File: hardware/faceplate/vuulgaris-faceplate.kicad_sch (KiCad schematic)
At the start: 7 parts, among them J1 HX JN2.54-2x5P TP H8.9, U1 MSP430FR2675TPT

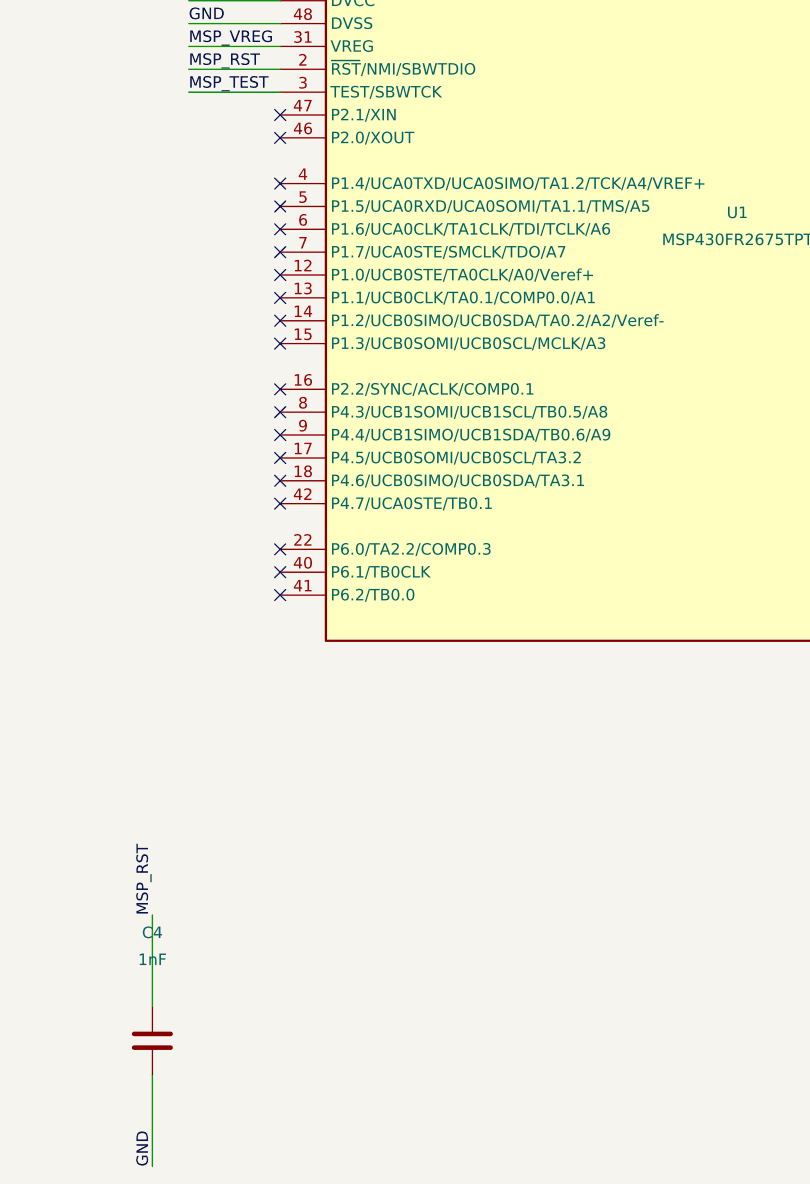
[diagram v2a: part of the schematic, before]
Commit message: faceplate: UART on P1.4/P1.5 with 47k pull-ups
U1 pin 4 (P1.4/UCA0TXD) on MSP430_TXD and pin 5 (P1.5/UCA0RXD) on
MSP430_RXD, the cable's J1.7 and J1.5 -- the default UCA0 pins, which are
also the UART BSL's (SLASEO5D Table 9-4, pin-allocation.md).

From TI: R2/R3 47k pull-ups, SLAU550 section 3.3.2.1, "Add a 47-kohm pullup
resistor and a 1-nF pulldown capacitor on TCK and TMS" (P1.4 is TCK, P1.5
TMS). Not fitted, by the decision in README section 6: the 1nF pulldowns,
which serve the hardware BSL entry sequence that production never uses.

Checked: mksch -> netcheck 31/31, 0 unintended, 7 nets; panelcheck 6 OK;
board untouched.
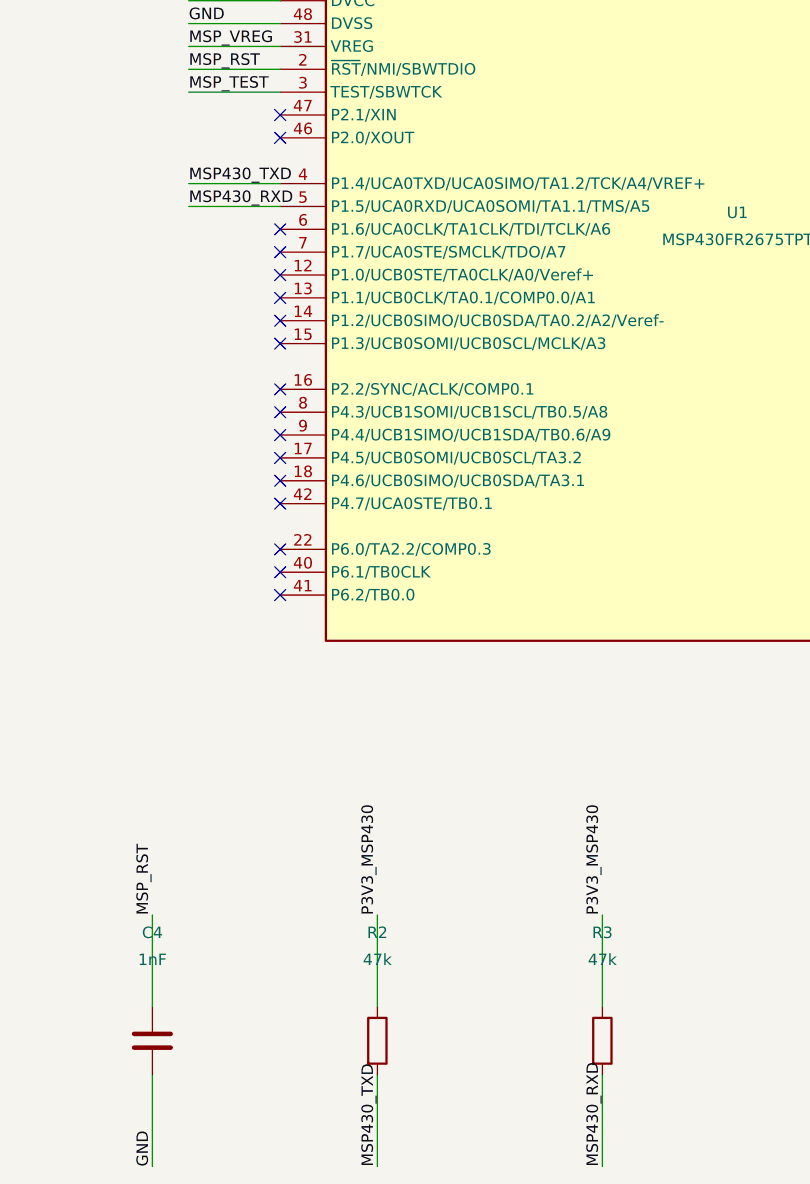
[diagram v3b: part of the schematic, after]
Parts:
- added R2, R3: 47k, vuulgaris:R0603, symbol vuulgaris:R
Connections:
- net MSP430_RXD: now also U1.5 (P1.5/UCA0RXD/UCA0SOMI/TA1.1/TMS/A5), R3.2
- net MSP430_TXD: now also U1.4 (P1.4/UCA0TXD/UCA0SIMO/TA1.2/TCK/A4/VREF+), R2.2
- net P3V3_MSP430: now also R2.1, R3.1
- no-connect marks 43 -> 41
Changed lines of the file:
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@@
+    (pin "2")
+  )
+  (symbol (lib_id "vuulgaris:R") (at 290 300 0) (unit 1)
+    (in_bom yes) (on_board yes) (dnp no)
+    (property "Reference" "R2" (at 290 288 0) (effects (font (size 1.27 1.27))))
+    (property "Value" "47k" (at 290 291 0) (effects (font (size 1.27 1.27))))
+    (property "Footprint" "vuulgaris:R0603" (at 290 300 0) (effects (font (size 1.27 1.27)) hide))
+    (property "Datasheet" "" (at 290 300 0) (effects (font (size 1.27 1.27)) hide))
+    (pin "1")
+    (pin "2")
+  )
+  (symbol (lib_id "vuulgaris:R") (at 315 300 0) (unit 1)
+    (in_bom yes) (on_board yes) (dnp no)
+    (property "Reference" "R3" (at 315 288 0) (effects (font (size 1.27 1.27))))
+    (property "Value" "47k" (at 315 291 0) (effects (font (size 1.27 1.27))))
+    (property "Footprint" "vuulgaris:R0603" (at 315 300 0) (effects (font (size 1.27 1.27)) hide))
+    (property "Datasheet" "" (at 315 300 0) (effects (font (size 1.27 1.27)) hide))
+    (pin "1")
     (pin "2")
   )
@@
   (wire (pts (xy 240.0 296.19) (xy 240.0 286.03)) (stroke (width 0) (type solid)))
   (wire (pts (xy 240.0 303.81) (xy 240.0 313.97)) (stroke (width 0) (type solid)))
+  (wire (pts (xy 290.0 296.19) (xy 290.0 286.03)) (stroke (width 0) (type solid)))
+  (wire (pts (xy 290.0 303.81) (xy 290.0 313.97)) (stroke (width 0) (type solid)))
+  (wire (pts (xy 315.0 296.19) (xy 315.0 286.03)) (stroke (width 0) (type solid)))
+  (wire (pts (xy 315.0 303.81) (xy 315.0 313.97)) (stroke (width 0) (type solid)))
   (wire (pts (xy 279.2 184.44) (xy 269.04 184.44)) (stroke (width 0) (type solid)))
   (wire (pts (xy 279.2 186.98) (xy 269.04 186.98)) (stroke (width 0) (type solid)))
@@
   (wire (pts (xy 279.2 192.06) (xy 269.04 192.06)) (stroke (width 0) (type solid)))
   (wire (pts (xy 279.2 194.6) (xy 269.04 194.6)) (stroke (width 0) (type solid)))
+  (wire (pts (xy 279.2 204.76) (xy 269.04 204.76)) (stroke (width 0) (type solid)))
+  (wire (pts (xy 279.2 207.3) (xy 269.04 207.3)) (stroke (width 0) (type solid)))
   (label "P3V3_MSP430" (at 160.0 286.03 90) (fields_autoplaced)
     (effects (font (size 1.27 1.27)) (justify left bottom))
@@
     (effects (font (size 1.27 1.27)) (justify left bottom))
   )
+  (label "P3V3_MSP430" (at 290.0 286.03 90) (fields_autoplaced)
+    (effects (font (size 1.27 1.27)) (justify left bottom))
+  )
+  (label "MSP430_TXD" (at 290.0 313.97 270) (fields_autoplaced)
+    (effects (font (size 1.27 1.27)) (justify left bottom))
+  )
+  (label "P3V3_MSP430" (at 315.0 286.03 90) (fields_autoplaced)
+    (effects (font (size 1.27 1.27)) (justify left bottom))
+  )
+  (label "MSP430_RXD" (at 315.0 313.97 270) (fields_autoplaced)
+    (effects (font (size 1.27 1.27)) (justify left bottom))
+  )
   (label "P3V3_MSP430" (at 269.04 184.44 180) (fields_autoplaced)
     (effects (font (size 1.27 1.27)) (justify left bottom))
@@
   )
   (label "MSP_TEST" (at 269.04 194.6 180) (fields_autoplaced)
+    (effects (font (size 1.27 1.27)) (justify left bottom))
+  )
+  (label "MSP430_TXD" (at 269.04 204.76 180) (fields_autoplaced)
+    (effects (font (size 1.27 1.27)) (justify left bottom))
+  )
+  (label "MSP430_RXD" (at 269.04 207.3 180) (fields_autoplaced)
     (effects (font (size 1.27 1.27)) (justify left bottom))
   )
   (no_connect (at 279.2 197.14))
   (no_connect (at 279.2 199.68))
-  (no_connect (at 279.2 204.76))
-  (no_connect (at 279.2 207.3))
   (no_connect (at 279.2 209.84))
   (no_connect (at 279.2 212.38))

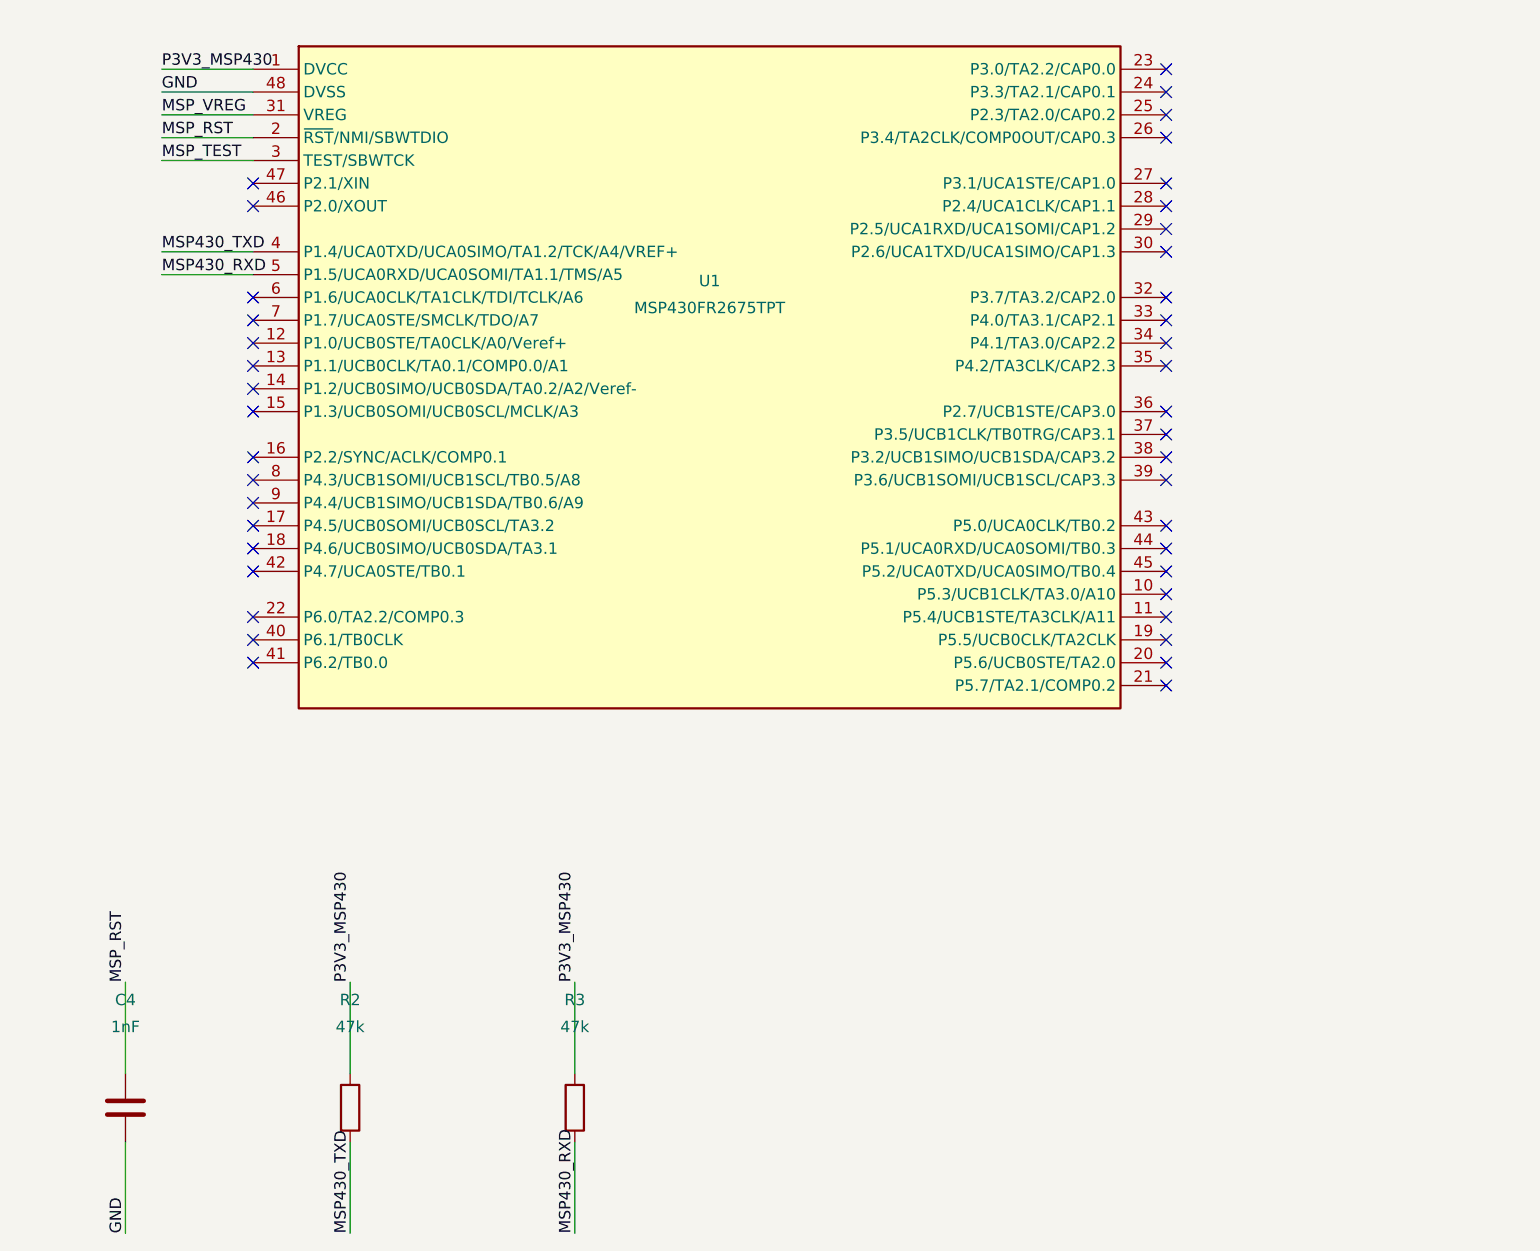
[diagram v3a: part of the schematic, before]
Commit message: faceplate: 32.768kHz crystal on XIN/XOUT (Q22)
Y1, Epson FC-135 32.768kHz 12.5pF (C32346, JLC Basic), on U1 pins 47
(P2.1/XIN) and 46 (P2.0/XOUT), C5/C6 22pF C0G from each pin to ground.

From a TI reference circuit: the topology, SLASEO5D section 10.1.2 /
Figure 10-2 -- crystal across XIN/XOUT, a capacitor from each to ground,
"External bypass capacitors for the crystal oscillator pins are required".
The crystal meets TI's limits in 8.12.3.1: a supported 12.5pF load, and C0
1pF against the 1.6pF maximum shunt capacitance.

NOT from a reference circuit: the capacitor value. TI gives none, only "meet
the effective load capacitance specified by crystal manufacturers", with
CL,eff 1pF integrated (8.12.3.1, read from the rendered table). 12.5pF less
1pF, doubled, less board stray is about 20pF; there is no Basic 20pF C0G 0603
at JLC (checked), so 22pF (C1653, already on the main board), a pF or so
high -- a few ppm of pull, irrelevant to a UART. Q22 updated; populating it
is still a later decision.

Checked: mksch -> netcheck 39/39, 0 unintended, 9 nets. Board untouched.
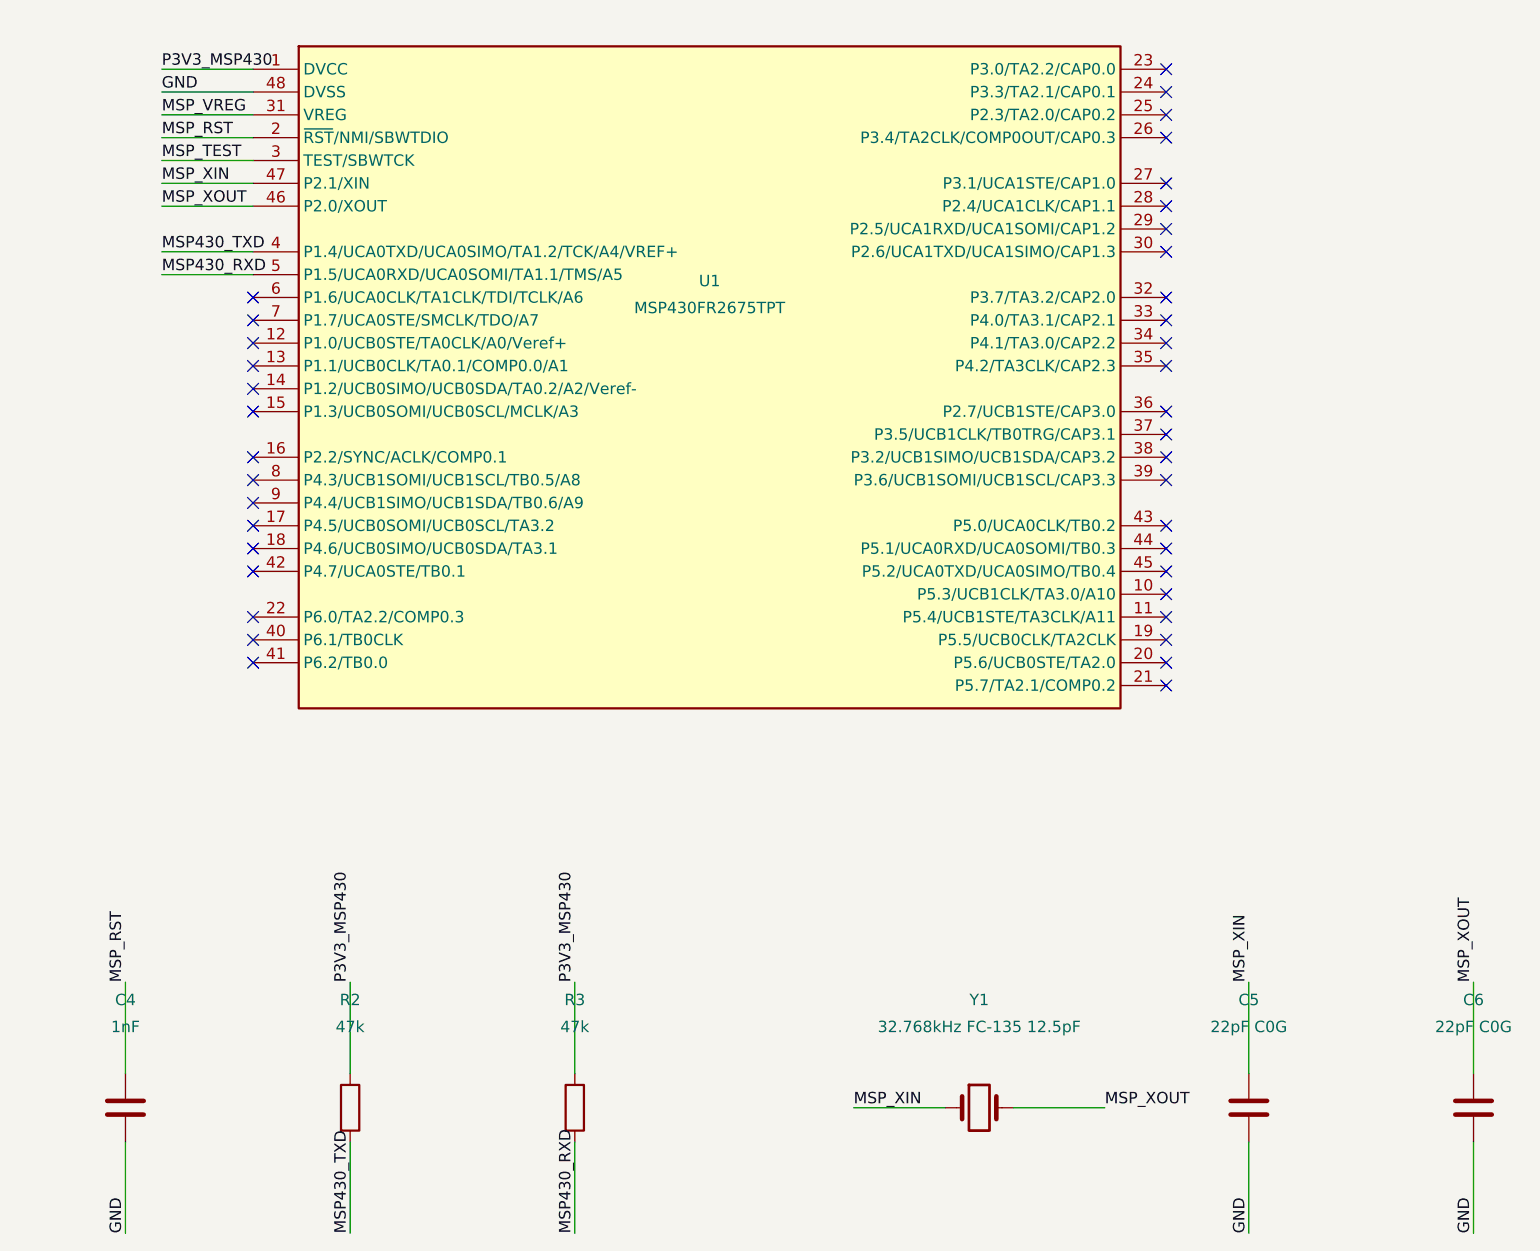
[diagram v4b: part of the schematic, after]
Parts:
- added C5, C6: 22pF C0G, vuulgaris:C0603, symbol vuulgaris:C
- added Y1: 32.768kHz FC-135 12.5pF, vuulgaris:XTAL-SMD_FC-135_3.2x1.5mm, symbol vuulgaris:Crystal
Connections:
- net GND: now also C5.2, C6.2
- net MSP_XOUT: now reaches U1.46 (P2.0/XOUT)
- net MSP_XOUT: now also C6.1, Y1.2
- net MSP_XIN: now reaches U1.47 (P2.1/XIN)
- net MSP_XIN: now also C5.1, Y1.1
- no-connect marks 41 -> 39
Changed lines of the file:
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@@
+    (pin "2")
+  )
+  (symbol (lib_id "vuulgaris:C") (at 390 300 0) (unit 1)
+    (in_bom yes) (on_board yes) (dnp no)
+    (property "Reference" "C5" (at 390 288 0) (effects (font (size 1.27 1.27))))
+    (property "Value" "22pF C0G" (at 390 291 0) (effects (font (size 1.27 1.27))))
+    (property "Footprint" "vuulgaris:C0603" (at 390 300 0) (effects (font (size 1.27 1.27)) hide))
+    (property "Datasheet" "" (at 390 300 0) (effects (font (size 1.27 1.27)) hide))
+    (pin "1")
+    (pin "2")
+  )
+  (symbol (lib_id "vuulgaris:C") (at 415 300 0) (unit 1)
+    (in_bom yes) (on_board yes) (dnp no)
+    (property "Reference" "C6" (at 415 288 0) (effects (font (size 1.27 1.27))))
+    (property "Value" "22pF C0G" (at 415 291 0) (effects (font (size 1.27 1.27))))
+    (property "Footprint" "vuulgaris:C0603" (at 415 300 0) (effects (font (size 1.27 1.27)) hide))
+    (property "Datasheet" "" (at 415 300 0) (effects (font (size 1.27 1.27)) hide))
+    (pin "1")
     (pin "2")
   )
@@
     (pin "21")
   )
+  (symbol (lib_id "vuulgaris:Crystal") (at 360 300 0) (unit 1)
+    (in_bom yes) (on_board yes) (dnp no)
+    (property "Reference" "Y1" (at 360 288 0) (effects (font (size 1.27 1.27))))
+    (property "Value" "32.768kHz FC-135 12.5pF" (at 360 291 0) (effects (font (size 1.27 1.27))))
+    (property "Footprint" "vuulgaris:XTAL-SMD_FC-135_3.2x1.5mm" (at 360 300 0) (effects (font (size 1.27 1.27)) hide))
+    (property "Datasheet" "" (at 360 300 0) (effects (font (size 1.27 1.27)) hide))
+    (pin "1")
+    (pin "2")
+  )
   (wire (pts (xy 160.0 296.19) (xy 160.0 286.03)) (stroke (width 0) (type solid)))
   (wire (pts (xy 160.0 303.81) (xy 160.0 313.97)) (stroke (width 0) (type solid)))
@@
   (wire (pts (xy 265.0 296.19) (xy 265.0 286.03)) (stroke (width 0) (type solid)))
   (wire (pts (xy 265.0 303.81) (xy 265.0 313.97)) (stroke (width 0) (type solid)))
+  (wire (pts (xy 390.0 296.19) (xy 390.0 286.03)) (stroke (width 0) (type solid)))
+  (wire (pts (xy 390.0 303.81) (xy 390.0 313.97)) (stroke (width 0) (type solid)))
+  (wire (pts (xy 415.0 296.19) (xy 415.0 286.03)) (stroke (width 0) (type solid)))
+  (wire (pts (xy 415.0 303.81) (xy 415.0 313.97)) (stroke (width 0) (type solid)))
   (wire (pts (xy 94.92 94.92) (xy 84.76 94.92)) (stroke (width 0) (type solid)))
   (wire (pts (xy 107.62 94.92) (xy 117.78 94.92)) (stroke (width 0) (type solid)))
@@
   (wire (pts (xy 279.2 204.76) (xy 269.04 204.76)) (stroke (width 0) (type solid)))
   (wire (pts (xy 279.2 207.3) (xy 269.04 207.3)) (stroke (width 0) (type solid)))
+  (wire (pts (xy 279.2 197.14) (xy 269.04 197.14)) (stroke (width 0) (type solid)))
+  (wire (pts (xy 279.2 199.68) (xy 269.04 199.68)) (stroke (width 0) (type solid)))
+  (wire (pts (xy 356.19 300.0) (xy 346.03 300.0)) (stroke (width 0) (type solid)))
+  (wire (pts (xy 363.81 300.0) (xy 373.97 300.0)) (stroke (width 0) (type solid)))
   (label "P3V3_MSP430" (at 160.0 286.03 90) (fields_autoplaced)
     (effects (font (size 1.27 1.27)) (justify left bottom))
@@
     (effects (font (size 1.27 1.27)) (justify left bottom))
   )
+  (label "MSP_XIN" (at 390.0 286.03 90) (fields_autoplaced)
+    (effects (font (size 1.27 1.27)) (justify left bottom))
+  )
+  (label "GND" (at 390.0 313.97 270) (fields_autoplaced)
+    (effects (font (size 1.27 1.27)) (justify left bottom))
+  )
+  (label "MSP_XOUT" (at 415.0 286.03 90) (fields_autoplaced)
+    (effects (font (size 1.27 1.27)) (justify left bottom))
+  )
+  (label "GND" (at 415.0 313.97 270) (fields_autoplaced)
+    (effects (font (size 1.27 1.27)) (justify left bottom))
+  )
   (label "MSP_TEST" (at 84.76 94.92 180) (fields_autoplaced)
     (effects (font (size 1.27 1.27)) (justify left bottom))
@@
     (effects (font (size 1.27 1.27)) (justify left bottom))
   )
-  (no_connect (at 279.2 197.14))
-  (no_connect (at 279.2 199.68))
+  (label "MSP_XIN" (at 269.04 197.14 180) (fields_autoplaced)
+    (effects (font (size 1.27 1.27)) (justify left bottom))
+  )
+  (label "MSP_XOUT" (at 269.04 199.68 180) (fields_autoplaced)
+    (effects (font (size 1.27 1.27)) (justify left bottom))
+  )
+  (label "MSP_XIN" (at 346.03 300.0 180) (fields_autoplaced)
+    (effects (font (size 1.27 1.27)) (justify left bottom))
+  )
+  (label "MSP_XOUT" (at 373.97 300.0 0) (fields_autoplaced)
+    (effects (font (size 1.27 1.27)) (justify left bottom))
+  )
   (no_connect (at 279.2 209.84))
   (no_connect (at 279.2 212.38))
